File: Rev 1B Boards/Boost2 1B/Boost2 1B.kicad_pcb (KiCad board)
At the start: 4 copper layers, 71.2 x 46 mm, 40 parts, among them J27 Banana 2P, J28 Banana 2P, Q1 BSC059N04LS6, Q2 BSC059N04LS6, U1 TPS43061

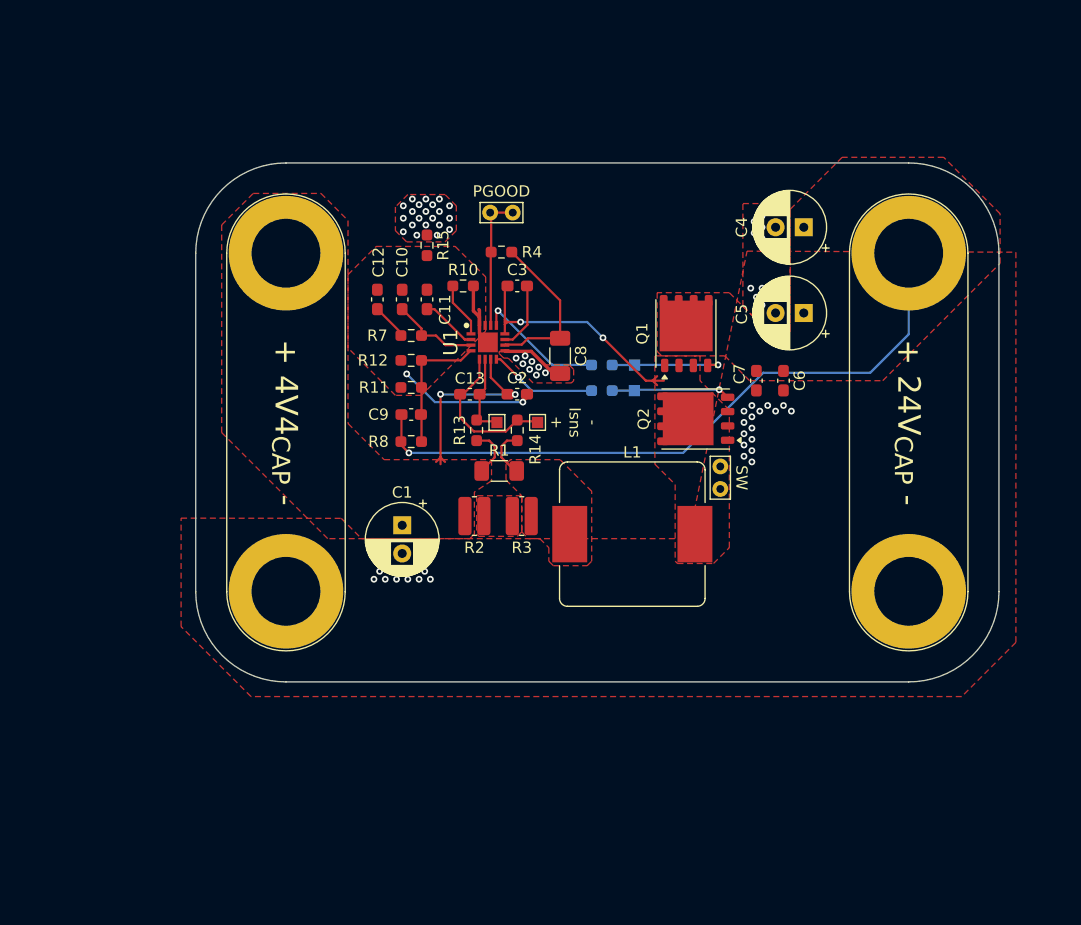
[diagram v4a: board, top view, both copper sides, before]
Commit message: Replace most banana jacks with XT connectors
+ update library
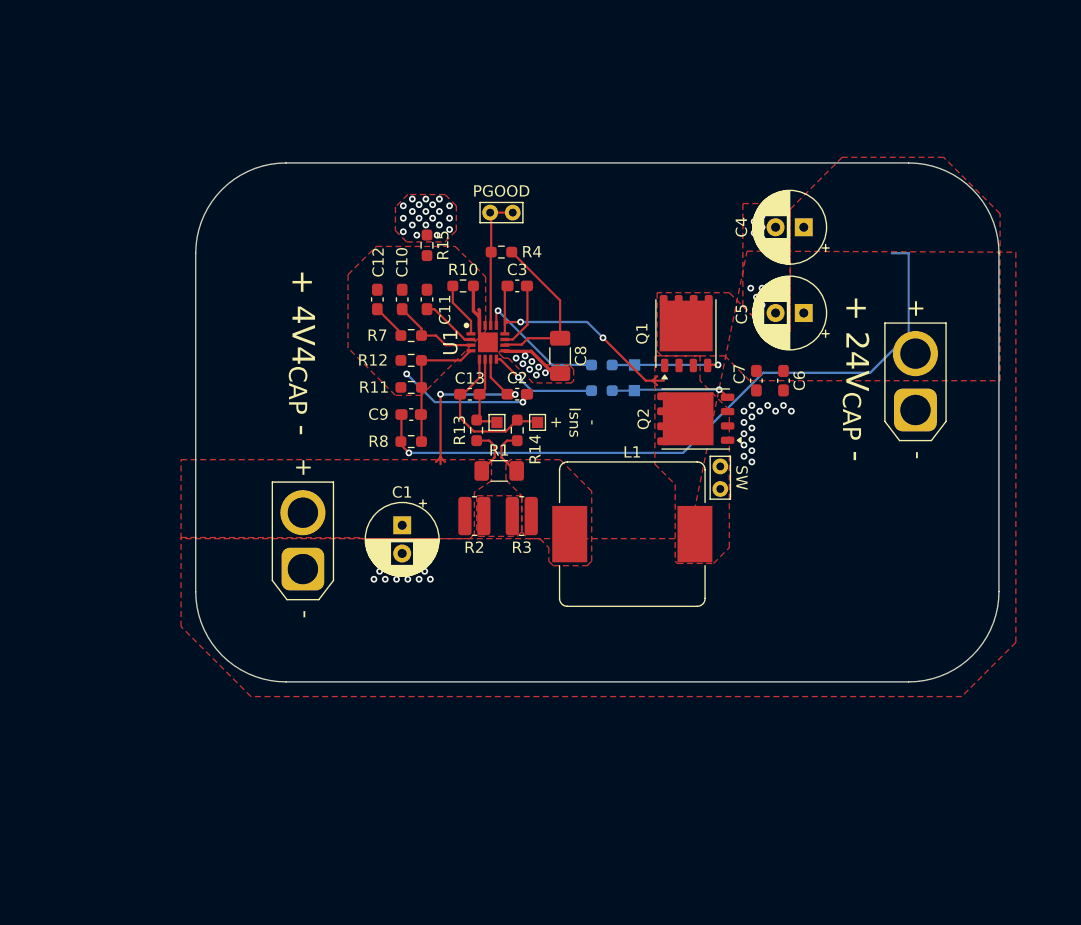
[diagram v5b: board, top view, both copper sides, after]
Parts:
- removed J27, J28: Banana 2P, Connector:Banana_Jack_2Pin
- added J3: XT30_F, Connector_AMASS:AMASS_XT30U-F_1x02_P5.0mm_Vertical, F.Cu at (107.4, 109.5)
- added J4: XT30_F, Connector_AMASS:AMASS_XT30U-F_1x02_P5.0mm_Vertical, F.Cu at (161.7, 95.4)
